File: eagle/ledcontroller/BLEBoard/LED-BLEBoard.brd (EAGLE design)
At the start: 38.4 x 31.7 mm, 18 parts, among them U1 FTSH-105-01-F-DV-ND, U2 RFD22301, U3 TPS61232, U4 V_REG_MIC2920, U5 7AAF-3

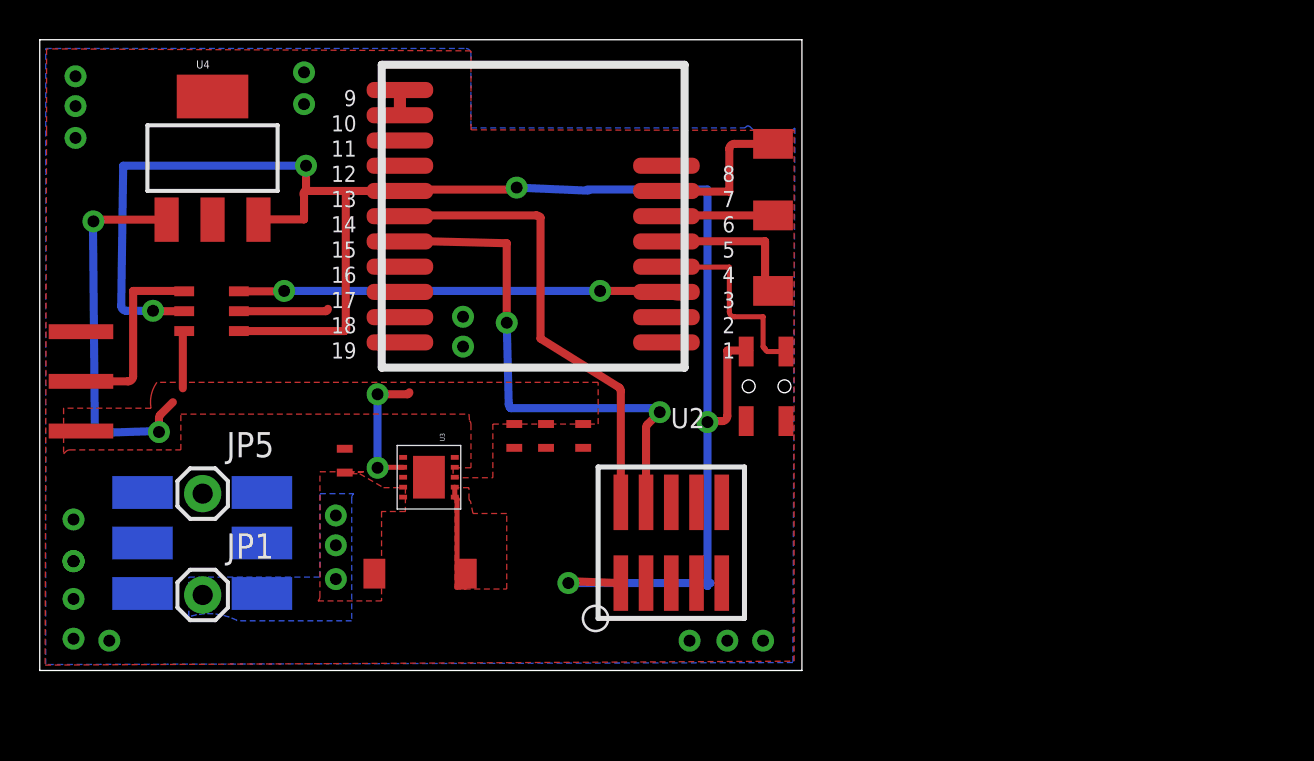
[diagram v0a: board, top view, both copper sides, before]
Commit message: LED 0.8 updates
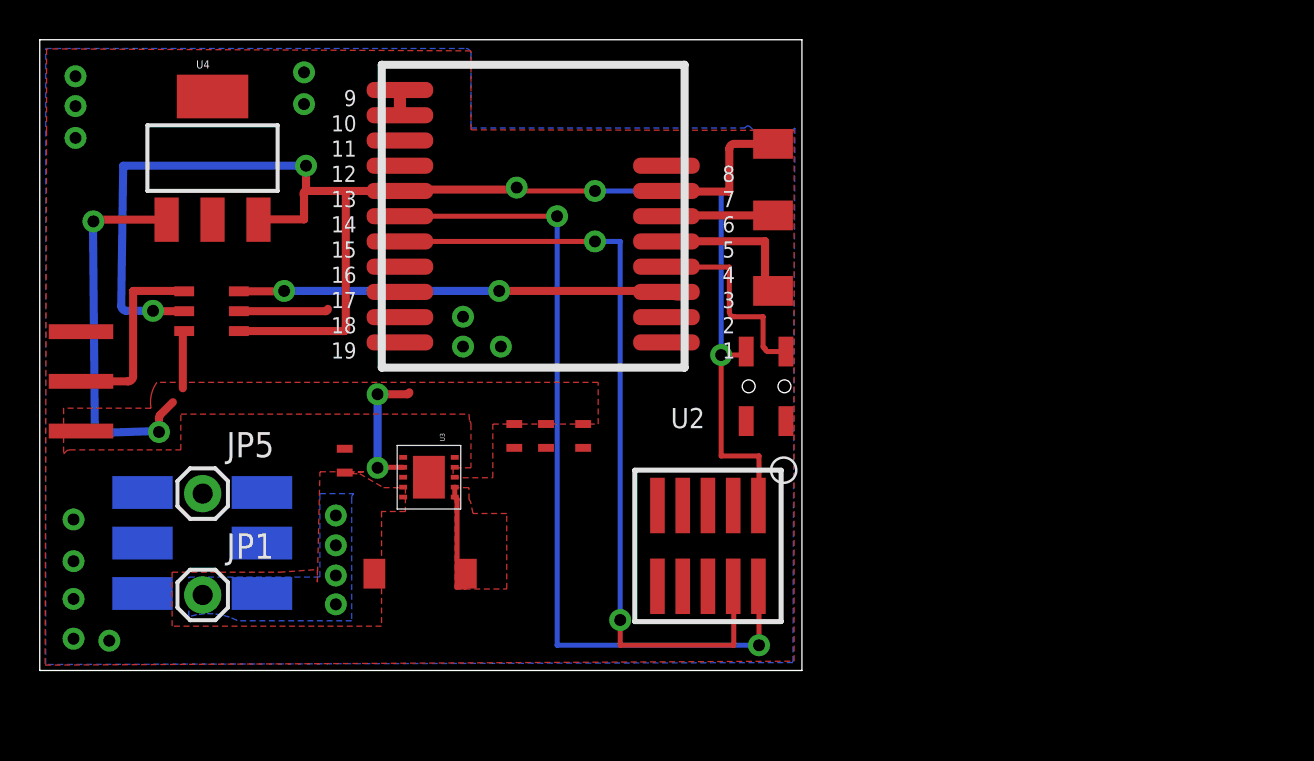
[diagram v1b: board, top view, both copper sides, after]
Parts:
- moved U1 1.85 mm to (33.6, 6.27), turned to 180 degrees
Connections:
- net 3.3V: no longer U$3.P$2
- net N$2: no longer U$3.P$4
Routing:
- net N$3: track 23.7 -> 42.7 mm, vias 0 -> 2
- net 3.3V: track 93.4 -> 77.5 mm
- net N$1: track 26.1 -> 40.1 mm
- net GND: vias 16 -> 13
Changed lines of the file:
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@@
 <setting verticaltext="up"/>
 </settings>
-<grid distance="0.05" unitdist="inch" unit="mm" style="lines" multiple="1" display="no" altdistance="0.025" altunitdist="inch" altunit="inch"/>
+<grid distance="1" unitdist="mm" unit="mm" style="lines" multiple="1" display="no" altdistance="0.25" altunitdist="mm" altunit="mm"/>
 <layers>
 <layer number="1" name="Top" color="4" fill="1" visible="yes" active="yes"/>
@@
 <element name="U3" library="bret" package="VSON10" value="TPS61232" x="19.585" y="9.725" rot="R90"/>
 <element name="U4" library="SparkFun-PowerIC" package="SOT223" value="V_REG_MIC2920" x="8.695" y="25.785"/>
-<element name="U1" library="bret" package="FTSH-105-01-XXX-DV-K" value="FTSH-105-01-F-DV-ND" x="31.78" y="6.43"/>
+<element name="U1" library="bret" package="FTSH-105-01-XXX-DV-K" value="FTSH-105-01-F-DV-ND" x="33.625" y="6.27" rot="R180"/>
 <element name="U2" library="RF_Digital_RFD22301_Eagle_Schematic_PCB_Library" package="RFD22301" value="RFD22301" x="24.83" y="24.13" rot="R180"/>
 <element name="U5" library="bret" package="70AAJ-3" value="7AAF-3" x="3.175" y="9.779" rot="MR90"/>
@@
 <via x="1.7" y="1.6" extent="1-16" drill="0.6"/>
 <via x="1.7" y="3.6" extent="1-16" drill="0.6"/>
-<via x="32.7" y="1.5" extent="1-16" drill="0.6"/>
-<via x="34.6" y="1.5" extent="1-16" drill="0.6"/>
-<via x="36.4" y="1.5" extent="1-16" drill="0.6"/>
 <wire x1="10.02" y1="18.08" x2="14.38" y2="18.08" width="0.4064" layer="1"/>
 <wire x1="14.38" y1="18.08" x2="14.5" y2="18.2" width="0.4064" layer="1" curve="90"/>
@@
 <via x="21.3" y="16.3" extent="1-16" drill="0.6"/>
 <via x="1.7" y="5.5" extent="1-16" drill="0.6"/>
-<via x="1.7" y="5.5" extent="1-16" drill="0.6"/>
 <via x="1.7" y="7.6" extent="1-16" drill="0.6"/>
 <via x="13.3" y="30.1" extent="1-16" drill="0.6"/>
 <via x="13.3" y="28.5" extent="1-16" drill="0.6"/>
+<via x="23.205" y="16.3" extent="1-16" drill="0.6"/>
 </signal>
 <signal name="PWR5V">
@@
 <vertex x="18.4" y="8"/>
 <vertex x="17.2" y="8"/>
-<vertex x="17.2" y="3.5"/>
-<vertex x="14" y="3.5"/>
-<vertex x="14.02560625" y="3.52560625" curve="44.999295"/>
-<vertex x="14.1" y="3.705209375"/>
+<vertex x="17.2" y="2.23"/>
+<vertex x="6.66" y="2.23"/>
+<vertex x="6.66" y="4.945"/>
+<vertex x="12.065" y="4.945"/>
+<vertex x="13.97" y="5.08"/>
+<vertex x="13.97" y="4.445"/>
 <vertex x="14.1" y="10"/>
 <vertex x="16.3" y="10"/>
@@
 <via x="14.9" y="7.8" extent="1-16" drill="0.6"/>
 <via x="14.9" y="6.3" extent="1-16" drill="0.6"/>
-<via x="14.9" y="4.6" extent="1-16" drill="0.6"/>
+<via x="14.9" y="3.33" extent="1-16" drill="0.6"/>
 <contactref element="JP1" pad="1"/>
+<via x="14.9" y="4.78" extent="1-16" drill="0.6"/>
 </signal>
 <signal name="3.3V">
@@
 <via x="13.4" y="25.4" extent="1-16" drill="0.6"/>
 <wire x1="13.4" y1="25.4" x2="13.4" y2="24.13" width="0.4064" layer="1"/>
-<wire x1="29.24" y1="4.398" x2="26.504828125" y2="4.498" width="0.4064" layer="1"/>
-<wire x1="26.504828125" y1="4.498" x2="26.6" y2="4.4" width="0.4064" layer="1" curve="-45"/>
-<via x="26.6" y="4.4" extent="1-16" drill="0.6"/>
-<wire x1="26.6" y1="4.4" x2="33.746" y2="4.4" width="0.4064" layer="16"/>
-<wire x1="33.746" y1="4.4" x2="33.6" y2="4.254" width="0.4064" layer="16" curve="90"/>
-<wire x1="33.6" y1="4.254" x2="33.6" y2="12.5" width="0.4064" layer="16"/>
-<wire x1="33.6" y1="12.5" x2="33.6" y2="24.2" width="0.4064" layer="16"/>
-<wire x1="33.6" y1="24.2" x2="27.554" y2="24.2" width="0.4064" layer="16"/>
-<wire x1="27.6" y1="24.146" x2="24" y2="24.3" width="0.4064" layer="16"/>
 <via x="24" y="24.3" extent="1-16" drill="0.6"/>
 <wire x1="18.1944" y1="24.2" x2="18.1244" y2="24.13" width="0.4064" layer="1" curve="90"/>
 <contactref element="U$3" pad="P$1"/>
-<wire x1="33.65" y1="12.55" x2="33.6" y2="12.5" width="0.4064" layer="1" curve="90"/>
-<via x="33.6" y="12.5" extent="1-16" drill="0.6"/>
 <wire x1="18.1944" y1="24.2" x2="23.746" y2="24.2" width="0.4064" layer="1"/>
 <wire x1="23.746" y1="24.2" x2="24" y2="24.454" width="0.4064" layer="1" curve="90"/>
 <wire x1="24" y1="24.454" x2="24" y2="24.3" width="0.4064" layer="1"/>
-<wire x1="33.65" y1="12.55" x2="34.346" y2="12.55" width="0.4064" layer="1"/>
-<wire x1="34.346" y1="12.55" x2="34.6" y2="12.804" width="0.4064" layer="1" curve="90"/>
-<wire x1="34.6" y1="12.804" x2="34.6" y2="16.1" width="0.4064" layer="1"/>
-<wire x1="34.6" y1="16.1" x2="35.7" y2="16.1" width="0.4064" layer="1"/>
-<wire x1="35.7" y1="16.1" x2="35.55" y2="16.05" width="0.4064" layer="1" curve="-90"/>
-<contactref element="U$3" pad="P$2"/>
-<wire x1="34.6" y1="12.804" x2="35.55" y2="12.55" width="0" layer="19" extent="1-1"/>
-<wire x1="27.6" y1="24.146" x2="27.554" y2="24.2" width="0" layer="19" extent="16-16"/>
+<wire x1="36.165" y1="8.302" x2="36.195" y2="8.302" width="0.254" layer="1"/>
+<wire x1="36.195" y1="8.302" x2="36.195" y2="10.795" width="0.254" layer="1"/>
+<wire x1="36.195" y1="10.795" x2="34.29" y2="10.795" width="0.254" layer="1"/>
+<wire x1="34.29" y1="10.795" x2="34.29" y2="15.875" width="0.254" layer="1"/>
+<wire x1="34.29" y1="15.875" x2="35.55" y2="15.875" width="0.254" layer="1"/>
+<wire x1="35.55" y1="15.875" x2="35.55" y2="16.05" width="0.254" layer="1"/>
+<via x="34.29" y="15.875" extent="1-16" drill="0.6"/>
+<wire x1="34.29" y1="15.875" x2="34.29" y2="24.13" width="0.254" layer="16"/>
+<wire x1="34.29" y1="24.13" x2="27.94" y2="24.13" width="0.254" layer="16"/>
+<via x="27.94" y="24.13" extent="1-16" drill="0.6"/>
+<wire x1="27.94" y1="24.13" x2="24" y2="24.13" width="0.254" layer="1"/>
+<wire x1="24" y1="24.13" x2="24" y2="24.3" width="0.254" layer="1"/>
 </signal>
 <signal name="N$1">
 <contactref element="U1" pad="SWCLK/TCK"/>
 <contactref element="U2" pad="15"/>
-<wire x1="30.51" y1="8.462" x2="30.51" y2="12.204790625" width="0.4064" layer="1"/>
-<wire x1="30.51" y1="12.204790625" x2="30.58439375" y2="12.38439375" width="0.4064" layer="1" curve="-44.999502"/>
-<wire x1="30.58439375" y1="12.38439375" x2="31.2" y2="13" width="0.4064" layer="1"/>
-<via x="31.2" y="13" extent="1-16" drill="0.6"/>
-<via x="23.5" y="17.5" extent="1-16" drill="0.6"/>
-<wire x1="23.5" y1="17.5" x2="23.5" y2="21.5" width="0.4064" layer="1"/>
-<wire x1="23.5" y1="21.5" x2="19.448540625" y2="21.6" width="0.4064" layer="1"/>
-<wire x1="19.448540625" y1="21.6" x2="18.1244" y2="21.59" width="0.4064" layer="1" curve="45"/>
-<wire x1="23.5" y1="17.5" x2="23.6" y2="13.405209375" width="0.4064" layer="16"/>
-<wire x1="23.6" y1="13.405209375" x2="23.67439375" y2="13.22560625" width="0.4064" layer="16" curve="44.999502"/>
-<wire x1="23.67439375" y1="13.22560625" x2="23.7" y2="13.2" width="0.4064" layer="16"/>
-<wire x1="23.7" y1="13.2" x2="30.894790625" y2="13.2" width="0.4064" layer="16"/>
-<wire x1="30.894790625" y1="13.2" x2="31.07439375" y2="13.12560625" width="0.4064" layer="16" curve="-44.999502"/>
-<wire x1="31.07439375" y1="13.12560625" x2="31.2" y2="13" width="0.4064" layer="16"/>
+<wire x1="34.895" y1="4.238" x2="34.925" y2="4.238" width="0.254" layer="1"/>
+<wire x1="34.925" y1="4.238" x2="34.925" y2="1.27" width="0.254" layer="1"/>
+<wire x1="34.925" y1="1.27" x2="29.21" y2="1.27" width="0.254" layer="1"/>
+<wire x1="29.21" y1="1.27" x2="29.21" y2="2.54" width="0.254" layer="1"/>
+<via x="29.21" y="2.54" extent="1-16" drill="0.6"/>
+<wire x1="29.21" y1="2.54" x2="29.21" y2="21.59" width="0.254" layer="16"/>
+<wire x1="29.21" y1="21.59" x2="27.94" y2="21.59" width="0.254" layer="16"/>
+<via x="27.94" y="21.59" extent="1-16" drill="0.6"/>
+<wire x1="27.94" y1="21.59" x2="18.1244" y2="21.59" width="0.254" layer="1"/>
 </signal>
 <signal name="N$3">
 <contactref element="U1" pad="SWDIO/TMS"/>
 <contactref element="U2" pad="14"/>
-<wire x1="29.24" y1="8.462" x2="29.24" y2="14.054790625" width="0.4064" layer="1"/>
-<wire x1="29.24" y1="14.054790625" x2="29.16560625" y2="14.23439375" width="0.4064" layer="1" curve="44.999502"/>
-<wire x1="29.16560625" y1="14.23439375" x2="25.2" y2="16.7" width="0.4064" layer="1"/>
-<wire x1="25.2" y1="16.7" x2="25.2" y2="22.794790625" width="0.4064" layer="1"/>
-<wire x1="18.22096875" y1="22.9" x2="18.1244" y2="22.86" width="0.4064" layer="1" curve="45"/>
-<wire x1="18.22096875" y1="22.9" x2="24.98958125" y2="22.9" width="0.4064" layer="1"/>
-<wire x1="24.98958125" y1="22.9" x2="25.169184375" y2="22.82560625" width="0.4064" layer="1" curve="-44.999502"/>
-<wire x1="25.169184375" y1="22.82560625" x2="25.2" y2="22.794790625" width="0.4064" layer="1"/>
+<wire x1="36.165" y1="4.238" x2="36.195" y2="4.238" width="0.254" layer="1"/>
+<wire x1="36.195" y1="4.238" x2="36.195" y2="1.27" width="0.254" layer="1"/>
+<via x="36.195" y="1.27" extent="1-16" drill="0.6"/>
+<wire x1="36.195" y1="1.27" x2="26.035" y2="1.27" width="0.254" layer="16"/>
+<wire x1="26.035" y1="1.27" x2="26.035" y2="22.86" width="0.254" layer="16"/>
+<via x="26.035" y="22.86" extent="1-16" drill="0.6"/>
+<wire x1="26.035" y1="22.86" x2="18.1244" y2="22.86" width="0.254" layer="1"/>
 </signal>
 <signal name="N$4">
@@
 <wire x1="12.28" y1="19.08" x2="12.3" y2="19.1" width="0.4064" layer="1" curve="90"/>
 <via x="12.3" y="19.1" extent="1-16" drill="0.6"/>
-<wire x1="12.3" y1="19.1" x2="28.2" y2="19.1" width="0.4064" layer="16"/>
-<via x="28.2" y="19.1" extent="1-16" drill="0.6"/>
-<wire x1="28.2" y1="19.1" x2="32.7856" y2="19.1" width="0.4064" layer="1"/>
+<wire x1="12.3" y1="19.1" x2="23.12" y2="19.1" width="0.4064" layer="16"/>
+<via x="23.12" y="19.1" extent="1-16" drill="0.6"/>
+<wire x1="23.12" y1="19.1" x2="32.7856" y2="19.1" width="0.4064" layer="1"/>
 <wire x1="32.7856" y1="19.1" x2="31.5356" y2="19.05" width="0.4064" layer="1" curve="-90"/>
 </signal>
@@
 <wire x1="34.7" y1="20.3" x2="31.5556" y2="20.3" width="0.254" layer="1"/>
 <wire x1="31.5556" y1="20.3" x2="31.5356" y2="20.32" width="0.254" layer="1" curve="-90"/>
-<contactref element="U$3" pad="P$4"/>
-<wire x1="37.55" y1="12.55" x2="37.55" y2="16.05" width="0" layer="19" extent="1-1"/>
 </signal>
 <signal name="GPIO6">

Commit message: V0.8 added switch and re-layout
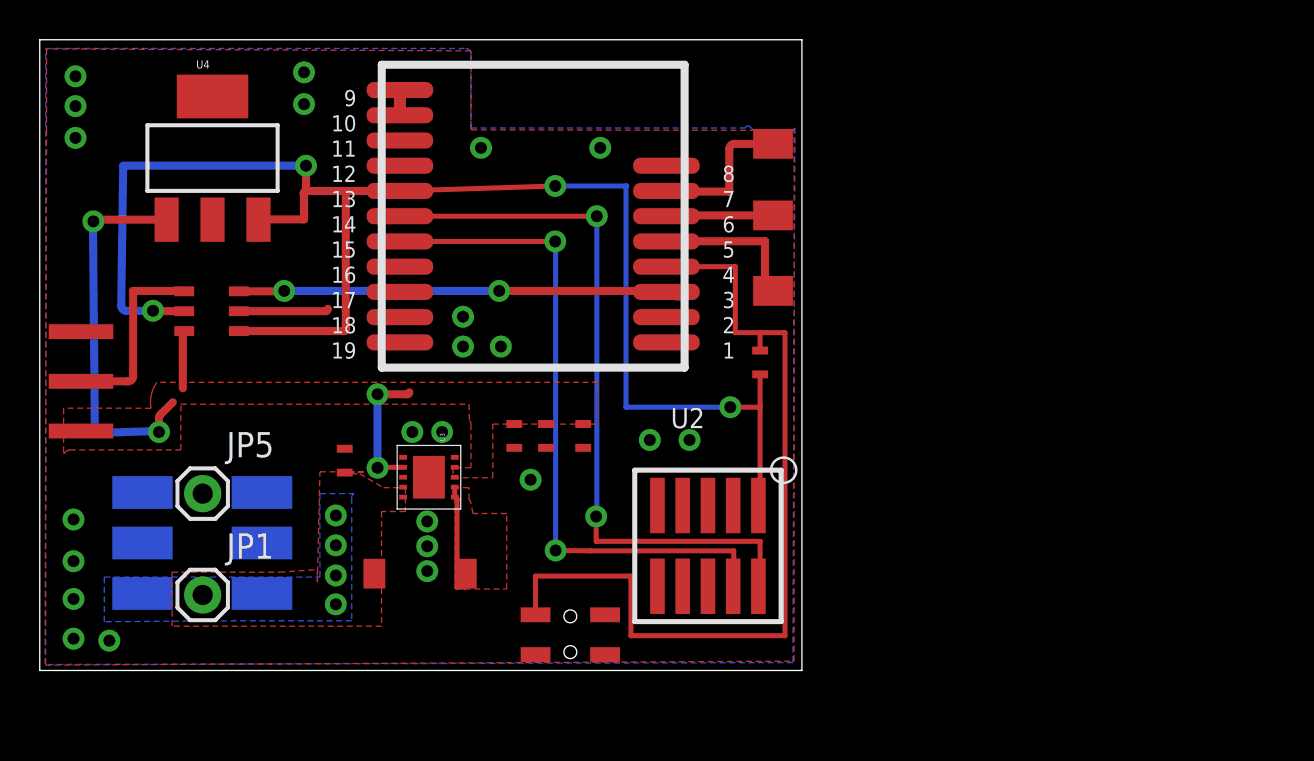
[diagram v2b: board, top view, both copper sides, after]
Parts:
- added U$4: MCR03ERTJ103, bret:C1.6X0.8
- moved U$3 12.8 mm to (29.2, 0.55), turned to 90 degrees
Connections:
- net 3.3V: now also U$4.IN; no longer U$3.P$1
- net GND: now also U$3.P$1, U5.P$3@1, U5.P$3@3; no longer U5.GND_OUT
- net N$2: now also U$4.OUT
- net VCC: now also U5.P$1@1, U5.P$1@2; no longer U5.P_OUT
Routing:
- net N$2: track 10.0 -> 42.9 mm
- net N$1: track 40.1 -> 34.2 mm
- net N$3: track 42.7 -> 36.9 mm
- net 3.3V: track 77.5 -> 77.8 mm, vias 5 -> 4
- net GND: vias 13 -> 23
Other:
- board text added: "C1"
- board text added: "LED Controller REV A"
- board text added: "R1"
- board text removed: "LED Controller V0.8"

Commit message: beginning
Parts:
- removed U4: V_REG_MIC2920, SparkFun-PowerIC:SOT223
- U5: value 7AAF-3 -> (none); device bret:70AAJ-3 -> bret:SC-74A-5PIN
- moved JP5 40.6 mm to (48.8, 10.0)
- moved U$4 35.0 mm to (2.50, 6.25), turned to 180 degrees
- moved U1 24.1 mm to (57.6, 4.27)
- moved U$3 23.2 mm to (6.00, 0.50)
- moved JP4 21.3 mm to (19.0, 15.0), turned to 180 degrees
- moved U2 18.6 mm to (37.0, 10.0)
- moved U$1 17.7 mm to (18.0, 0.40), turned to 0 degrees
- moved JP3 16.9 mm to (22.0, 15.0), turned to 180 degrees
- moved U$2 16.2 mm to (23.5, 8.42), turned to 270 degrees
- moved U5 16.1 mm to (19.0, 7.00), flipped to the top, turned to 270 degrees
- moved JP2 12.6 mm to (25.0, 15.0), turned to 180 degrees
- moved C3 12.0 mm to (16.0, 8.00), turned to 270 degrees
- moved C2 11.6 mm to (14.5, 8.00), turned to 270 degrees
- moved C4 11.5 mm to (13.0, 8.00), turned to 270 degrees
- moved L1 10.2 mm to (9.14, 2.87)
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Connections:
- net 3.3V: now also U5.P$5; no longer U4.3
- net GND: now also U5.P$2; no longer U4.2, U5.P$3@1, U5.P$3@3
- net PWR5V: now also U5.P$1, U5.P$3; no longer U4.1
- net VCC: no longer U5.P$1@1, U5.P$1@2
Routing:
- net 3.3V: track 77.8 -> 0.00 mm, vias 4 -> 0
- net N$2: track 42.9 -> 0.00 mm
- net N$3: track 36.9 -> 0.00 mm, vias 2 -> 0
- net N$1: track 34.2 -> 0.00 mm, vias 2 -> 0
- net PWR5V: track 29.7 -> 0.00 mm, vias 4 -> 0
- net GPIO2: track 24.0 -> 0.00 mm, vias 2 -> 0
- net N$10: track 9.60 -> 0.00 mm
- net GPIO4: track 7.72 -> 0.00 mm
- net GPIO6: track 7.63 -> 0.00 mm
- net PWIND: track 6.16 -> 0.50 mm
- net GPIO5: track 5.38 -> 0.00 mm
- net GND: track 5.80 -> 1.27 mm, vias 23 -> 0
- removed copper zone on layer 1, net PWIND
- removed copper zone on layer 1, net PWR5V
- removed copper zone on layer 1, net VCC
- removed copper zone on layer 16, net VCC
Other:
- board size 38.4 x 31.7 mm -> 52 x 17 mm
- board text removed: "2.3-5.5v"
- board text removed: "C1"
- board text removed: "Copyright 2015, Bret Patterson"
- board text removed: "GND"
- board text removed: "GPIO4"
- board text removed: "GPIO5"
- board text removed: "GPIO6"
- board text removed: "LED Controller REV A"
